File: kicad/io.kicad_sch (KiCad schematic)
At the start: 14 parts, among them J4 DE9_Plug_MountingHoles, J5 DB25_Receptacle_MountingHoles, U29 6522, U30 6551, U31 6551, U32 MAX232, U34 24LC256, X2 ACO-1.8432MHz-A

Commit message: Add caps and make initial placement
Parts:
- added C38, C39, C40, C41, C42, C43: 100n, Capacitor_THT:C_Disc_D5.0mm_W2.5mm_P2.50mm, symbol Device:C
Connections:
- net GND: now also C38.2, C39.2, C40.2, C41.2, C42.2, C43.2
- net VCC: now also C38.1, C39.1, C40.1, C41.1, C42.1, C43.1

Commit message: Bugfixes, start routing
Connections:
- net GND: now also J5.22 (P22), J5.23 (P23)
- net ROMSEL0: now reaches U29.14 (PB4)
- net ROMSEL0: no longer J5.22 (P22)
- net ROMSEL1: now reaches U29.15 (PB5)
- net ROMSEL1: no longer J5.23 (P23)
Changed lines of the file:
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@@
 	)
 	(junction
+		(at 80.01 97.79)
+		(diameter 0)
+		(color 0 0 0 0)
+	)
+	(junction
 		(at 242.57 26.67)
 		(diameter 0)
@@
 	)
 	(junction
+		(at 80.01 92.71)
+		(diameter 0)
+		(color 0 0 0 0)
+	)
+	(junction
 		(at 35.56 138.43)
 		(diameter 0)
@@
 	(wire
 		(pts
+			(xy 80.01 97.79) (xy 80.01 92.71)
+		)
+		(stroke
+			(width 0)
+			(type default)
+		)
+	)
+	(wire
+		(pts
 			(xy 137.16 114.3) (xy 148.59 114.3)
 		)
@@
 	(wire
 		(pts
-			(xy 66.04 92.71) (xy 66.04 97.79)
+			(xy 66.04 92.71) (xy 66.04 119.38)
 		)
 		(stroke
@@
 	(wire
 		(pts
+			(xy 80.01 97.79) (xy 82.55 97.79)
+		)
+		(stroke
+			(width 0)
+			(type default)
+		)
+	)
+	(wire
+		(pts
 			(xy 35.56 162.56) (xy 24.13 162.56)
 		)
@@
 	(wire
 		(pts
+			(xy 80.01 92.71) (xy 82.55 92.71)
+		)
+		(stroke
+			(width 0)
+			(type default)
+		)
+	)
+	(wire
+		(pts
 			(xy 63.5 73.66) (xy 69.85 73.66)
 		)
@@
 		)
 	)
+	(wire
+		(pts
+			(xy 66.04 119.38) (xy 68.58 119.38)
+		)
+		(stroke
+			(width 0)
+			(type default)
+		)
+	)
 	(bus
 		(pts
@@
 	(wire
 		(pts
+			(xy 67.31 116.84) (xy 68.58 116.84)
+		)
+		(stroke
+			(width 0)
+			(type default)
+		)
+	)
+	(wire
+		(pts
 			(xy 265.43 128.27) (xy 262.89 128.27)
 		)
@@
 	(wire
 		(pts
-			(xy 66.04 97.79) (xy 82.55 97.79)
-		)
-		(stroke
-			(width 0)
-			(type default)
-		)
-	)
-	(wire
-		(pts
 			(xy 255.27 154.94) (xy 265.43 154.94)
 		)
@@
 		)
 	)
-	(wire
-		(pts
-			(xy 67.31 92.71) (xy 82.55 92.71)
-		)
-		(stroke
-			(width 0)
-			(type default)
-		)
-	)
 	(bus
 		(pts
@@
 	(wire
 		(pts
-			(xy 80.01 115.57) (xy 80.01 107.95)
+			(xy 80.01 113.03) (xy 80.01 107.95)
 		)
 		(stroke
@@
 	(wire
 		(pts
+			(xy 80.01 92.71) (xy 80.01 57.15)
+		)
+		(stroke
+			(width 0)
+			(type default)
+		)
+	)
+	(wire
+		(pts
 			(xy 209.55 104.14) (xy 222.25 104.14)
 		)
@@
 	(wire
 		(pts
-			(xy 80.01 100.33) (xy 80.01 57.15)
+			(xy 80.01 100.33) (xy 80.01 97.79)
 		)
 		(stroke
@@
 		)
 	)
-	(bus
+	(wire
 		(pts
-			(xy 34.29 95.25) (xy 34.29 97.79)
+			(xy 67.31 90.17) (xy 67.31 116.84)
 		)
 		(stroke
@@
 		)
 	)
-	(wire
+	(bus
 		(pts
-			(xy 67.31 90.17) (xy 67.31 92.71)
+			(xy 34.29 95.25) (xy 34.29 97.79)
 		)
 		(stroke
@@
 		)
 	)
+	(hierarchical_label "ROMSEL1"
+		(shape output)
+		(at 68.58 119.38 0)
+		(fields_autoplaced yes)
+		(effects
+			(font
+				(size 1.27 1.27)
+			)
+			(justify left)
+		)
+	)
+	(hierarchical_label "ROMSEL0"
+		(shape output)
+		(at 68.58 116.84 0)
+		(fields_autoplaced yes)
+		(effects
+			(font
+				(size 1.27 1.27)
+			)
+			(justify left)
+		)
+	)
 	(hierarchical_label "R{slash}W"
 		(shape input)
@@
 	(symbol
 		(lib_id "power:GND")
-		(at 80.01 115.57 0)
+		(at 80.01 113.03 0)
 		(unit 1)
 		(exclude_from_sim no)
@@
 		(on_board yes)
 		(dnp no)
-		(fields_autoplaced yes)
 		(property "Reference" "#PWR074"
-			(at 80.01 121.92 0)
+			(at 80.01 119.38 0)
 			(effects
 				(font
@@
 		)
 		(property "Value" "GND"
-			(at 80.01 120.65 0)
+			(at 83.312 114.808 0)
 			(effects
 				(font
@@
 		)
 		(property "Footprint" ""
-			(at 80.01 115.57 0)
+			(at 80.01 113.03 0)
 			(effects
 				(font
@@
 		)
 		(property "Datasheet" ""
-			(at 80.01 115.57 0)
+			(at 80.01 113.03 0)
 			(effects
 				(font
@@
 		)
 		(property "Description" "Power symbol creates a global label with name \"GND\" , ground"
-			(at 80.01 115.57 0)
+			(at 80.01 113.03 0)
 			(effects
 				(font

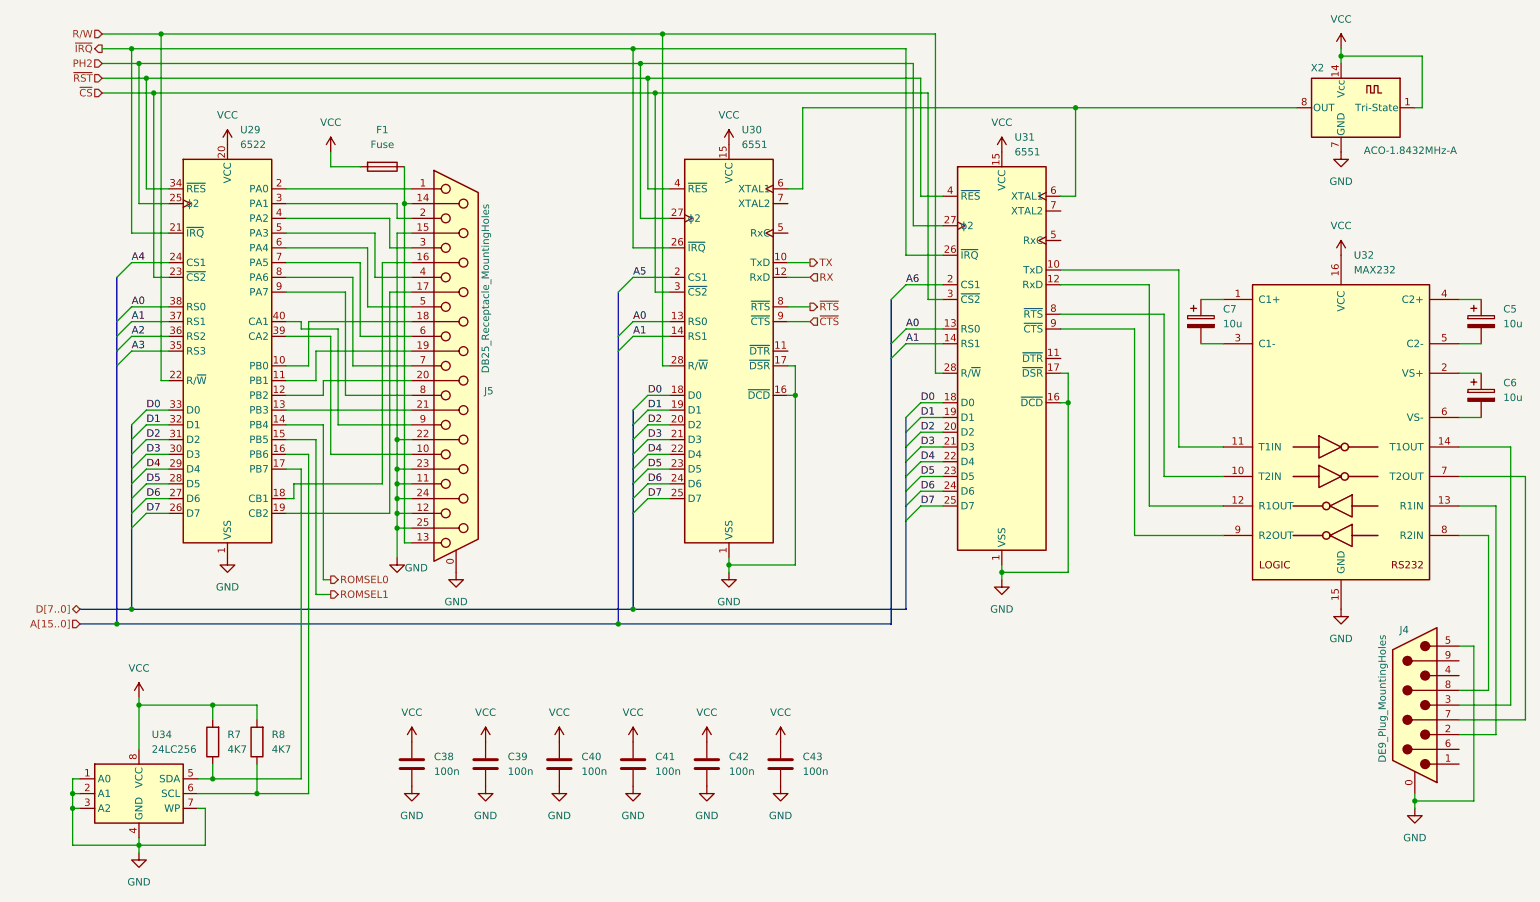
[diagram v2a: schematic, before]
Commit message: hw: revision C
Major changes:
- ROM space has been extended from 16 KiB to 32 KiB
- dynamic RAM option has been removed
- RAM size has been reduced from 32 KiB to 24 KiB
- expansion slot now replaces internal ROM, does not
  have dedicated memory space anymore
- place all I/O within a compactish 8 KiB
- move PH2 gating to /RD and /WR signals
- PCB redo (mechanicaly compatible)
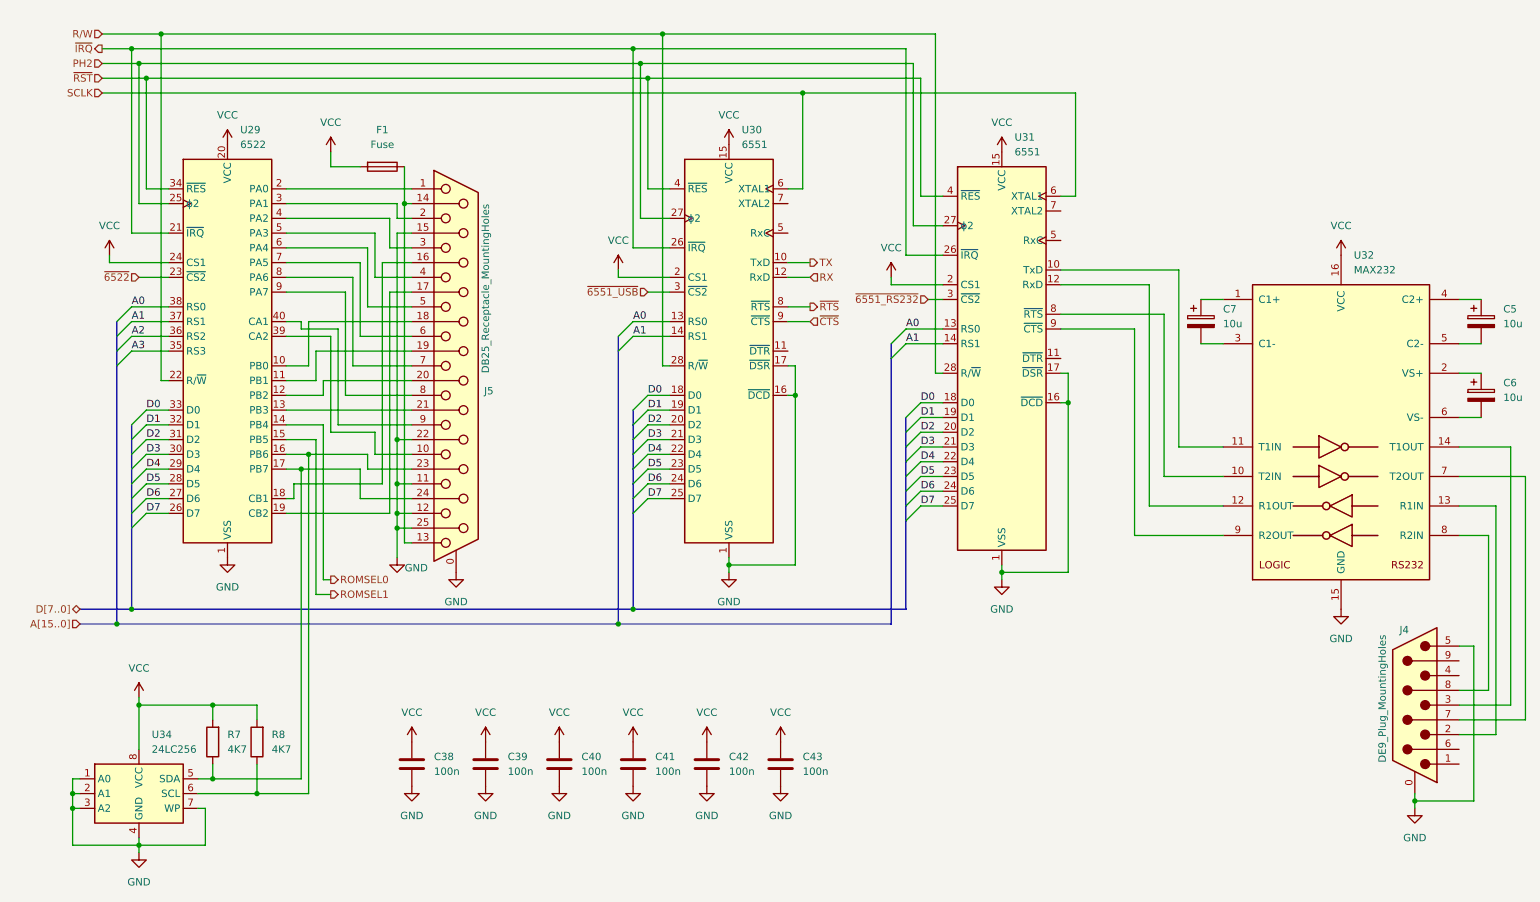
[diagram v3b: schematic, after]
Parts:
- removed X2: ACO-1.8432MHz-A, Oscillator:Oscillator_DIP-14, symbol Oscillator:ACO-xxxMHz-A
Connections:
- net A4 is gone; now on net VCC: U29.24 (CS1)
- net A5 is gone; now on net VCC: U30.2 (CS1)
- net A6 is gone; now on net VCC: U31.2 (CS1)
- net GND: no longer J5.23 (P23), J5.24 (P24)
- net SCLK: now reaches U30.6 (XTAL1), U31.6 (XTAL1)
- net at R7.1, U29.17 (PB7), U34.5 (SDA): now also J5.24 (P24)
- net at R8.1, U29.16 (PB6), U34.6 (SCL): now also J5.23 (P23)
- removed net ~{CS}: U29.23 (~{CS2}), U30.3 (~{CS2}), U31.3 (~{CS2})
- new net ~{6522}: U29.23 (~{CS2})
- new net ~{6551_RS232}: U31.3 (~{CS2})
- new net ~{6551_USB}: U30.3 (~{CS2})

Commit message: hw: rev D - replace DB25 connector footprint with available one
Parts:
- J5: footprint Connector_Dsub:DSUB-25_Female_Horizontal_P2.77x2.84mm_EdgePinOffset9.90mm_Housed_MountingHolesOffset11.32mm -> Connector_Dsub:DSUB-25_Socket_Horizontal_P2.77x2.84mm_EdgePinOffset7.70mm_Housed_MountingHolesOffset9.12mm
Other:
- company: (none) -> A.K.
- title: (none) -> Input/Output
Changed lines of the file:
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@@
 (kicad_sch
-	(version 20231120)
+	(version 20250114)
 	(generator "eeschema")
-	(generator_version "8.0")
+	(generator_version "9.0")
 	(paper "A4")
+	(title_block
+		(title "Input/Output")
+		(date "2025-08-04")
+		(rev "D")
+		(company "A.K.")
+	)
 	(junction
 		(at 48.26 138.43)
@@
 			)
 		)
-		(property "Footprint" "Connector_Dsub:DSUB-25_Female_Horizontal_P2.77x2.84mm_EdgePinOffset9.90mm_Housed_MountingHolesOffset11.32mm"
+		(property "Footprint" "Connector_Dsub:DSUB-25_Socket_Horizontal_P2.77x2.84mm_EdgePinOffset7.70mm_Housed_MountingHolesOffset9.12mm"
 			(at 90.17 80.01 0)
 			(effects
@@
 			)
 		)
-		(property "Datasheet" " ~"
+		(property "Datasheet" "~"
 			(at 90.17 80.01 0)
 			(effects
